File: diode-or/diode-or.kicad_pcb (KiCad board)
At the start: 2 copper layers, 80.4 x 51.4 mm, 24 parts, among them J1 Conn_01x01, J2 Conn_01x01, J3 Conn_01x01, J4 Conn_01x01, J5 Conn_01x01, Q1 Q_NMOS_GDS, SW1 SW_SPDT, U1 LM5050-1

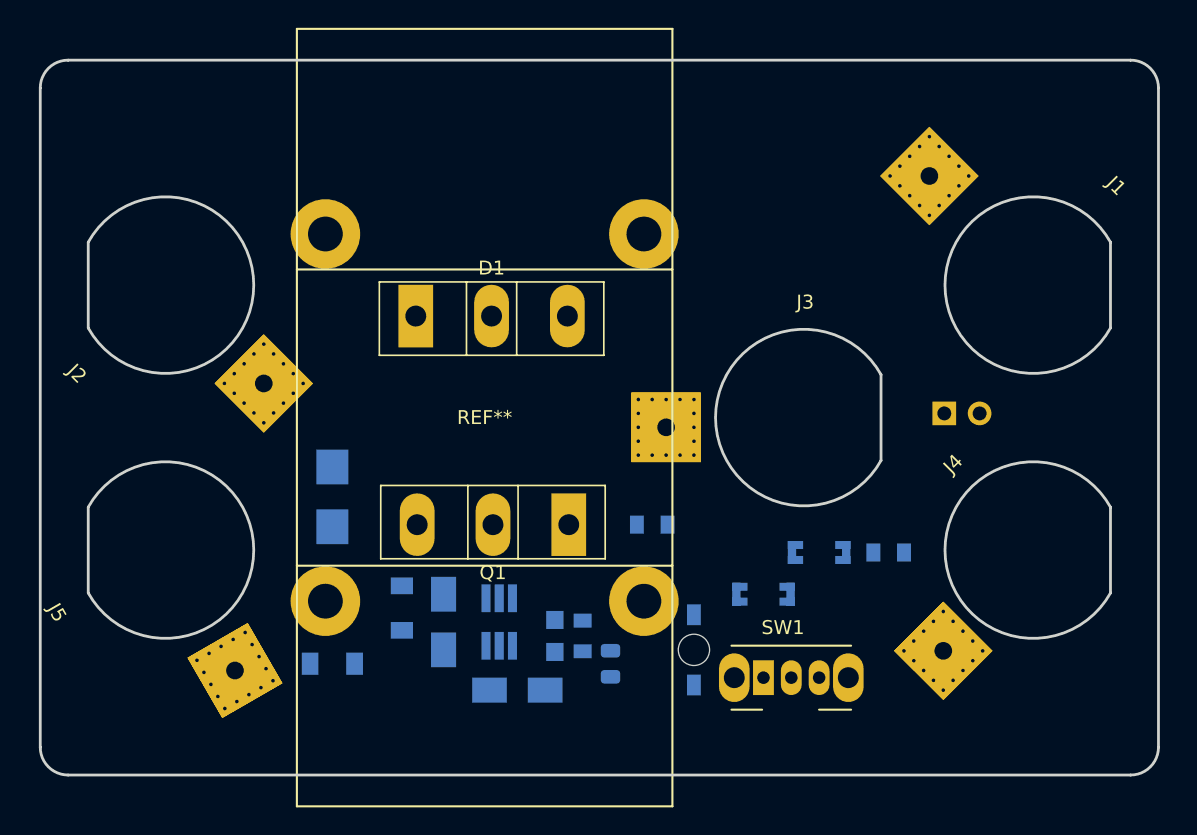
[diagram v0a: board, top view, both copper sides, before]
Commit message: Routed diode-or board. Add generated files.
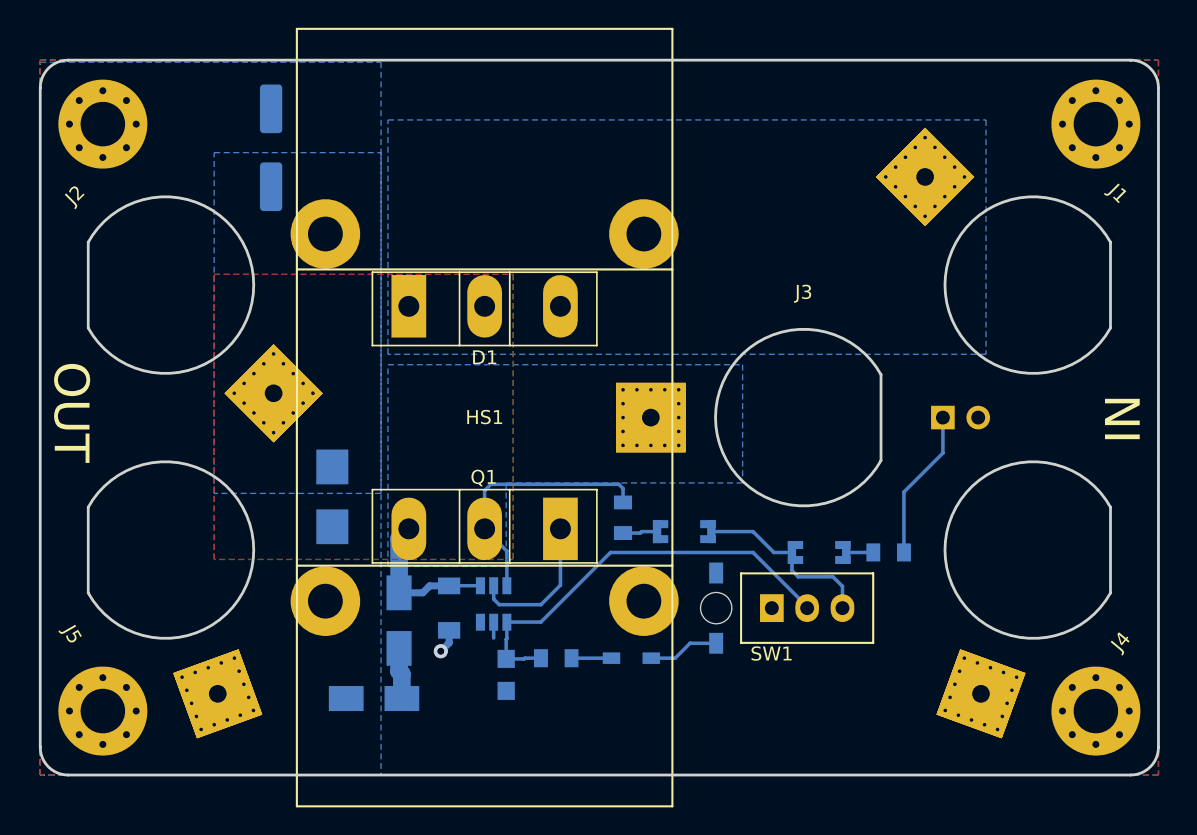
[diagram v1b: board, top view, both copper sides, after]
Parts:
- removed REF**: MA-301-27E, local:MA-301-27E
- added H1: MountingHole_Pad, MountingHole:MountingHole_3.2mm_M3_Pad_Via, F.Cu at (124.5, 73.2)
- added H2: MountingHole_Pad, MountingHole:MountingHole_3.2mm_M3_Pad_Via, F.Cu at (195.9, 73.2)
- added H3: MountingHole_Pad, MountingHole:MountingHole_3.2mm_M3_Pad_Via, F.Cu at (124.5, 115.4)
- added H4: MountingHole_Pad, MountingHole:MountingHole_3.2mm_M3_Pad_Via, F.Cu at (195.9, 115.4)
- added HS1: Heatsink_Pad, local:MA-301-27E, F.Cu at (152.0, 94.3)
- C1: footprint local:C_1206_HandSoldering -> Capacitor_SMD:CP_Elec_6.3x5.9
- C3: value 10uF -> 1uF
- D7: value D_Zener -> MM3Z4V3T1G; footprint Diode_SMD:D_0805_2012Metric -> local:SOD-323_477-02-H_HandSoldering
- J1, J2, J3: value Conn_01x01 -> Binding Post (RED)
- J4, J5: value Conn_01x01 -> Binding Post (BLACK)
- Q1: value Q_NMOS_GDS -> IRFP4710PBF
- SW1: footprint Button_Switch_THT:SW_CuK_OS102011MA1QN1_SPDT_Angled -> local:ASE1D-2M-10-Z
- U1: footprint Package_TO_SOT_SMD:TSOT-23-6_HandSoldering -> Package_TO_SOT_SMD:TSOT-23-6
- moved C1 37.4 mm to (136.6, 74.9), turned to 90 degrees
- moved D6 10.3 mm to (144.0, 114.5), turned to 0 degrees
- moved D3 7.26 mm to (166.3, 102.5)
- moved SW1 5.04 mm to (172.6, 108.0)
- moved C2 4.48 mm to (153.5, 112.8)
- moved C3 3.40 mm to (149.4, 108.0)
- moved D8 3.40 mm to (168.6, 108.0)
- moved D4 3.20 mm to (145.8, 108.9)
- moved R3 2.48 mm to (157.1, 111.6), turned to 0 degrees
- moved R1 2.16 mm to (161.9, 101.5), turned to 270 degrees
- moved D7 1.55 mm to (162.5, 111.6), turned to 0 degrees
- moved U1 1.36 mm to (152.6, 107.7)
- moved J1 0.87 mm to (191.4, 84.8)
- moved D1 0.86 mm to (146.5, 86.3)
- moved J3 0.71 mm to (174.9, 94.3)
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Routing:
- net /VS: track 0.00 -> 30.6 mm
- net /OUT_P: track 0.00 -> 18.8 mm
- net /VS_OR: track 0.00 -> 13.4 mm
- net /IN_FET_P: track 0.00 -> 11.0 mm
- net /BATT: track 0.00 -> 10.9 mm
- net /GATE: track 0.00 -> 10.6 mm
- net Net-(D7-Pad2): track 0.00 -> 5.12 mm
- net GND: track 0.00 -> 4.82 mm
- net Net-(D7-Pad1): track 0.00 -> 2.87 mm
- net Net-(D3-Pad2): track 0.00 -> 2.49 mm
- net Net-(D5-Pad2): track 0.00 -> 1.95 mm
- net /IN_OUT_N: track 0.00 -> 1.75 mm, vias 0 -> 1
- added copper zone on B.Cu, net /IN_D_P
- added copper zone on B.Cu, net /IN_FET_P
- added copper zone on B.Cu, net /IN_OUT_N
- added copper zone on F.Cu, net /IN_OUT_N
- added copper zone on B.Cu, net /OUT_P
- added copper zone on F.Cu, net /OUT_P
- added copper zone on B.Cu, net GND
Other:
- net class Power added: clearance 0.635, trace_width 0.254, via_dia 0.762, via_drill 0.381
- board text added: "IN"
- board text added: "OUT"

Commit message: Changes to courtyard and pad connection settings.
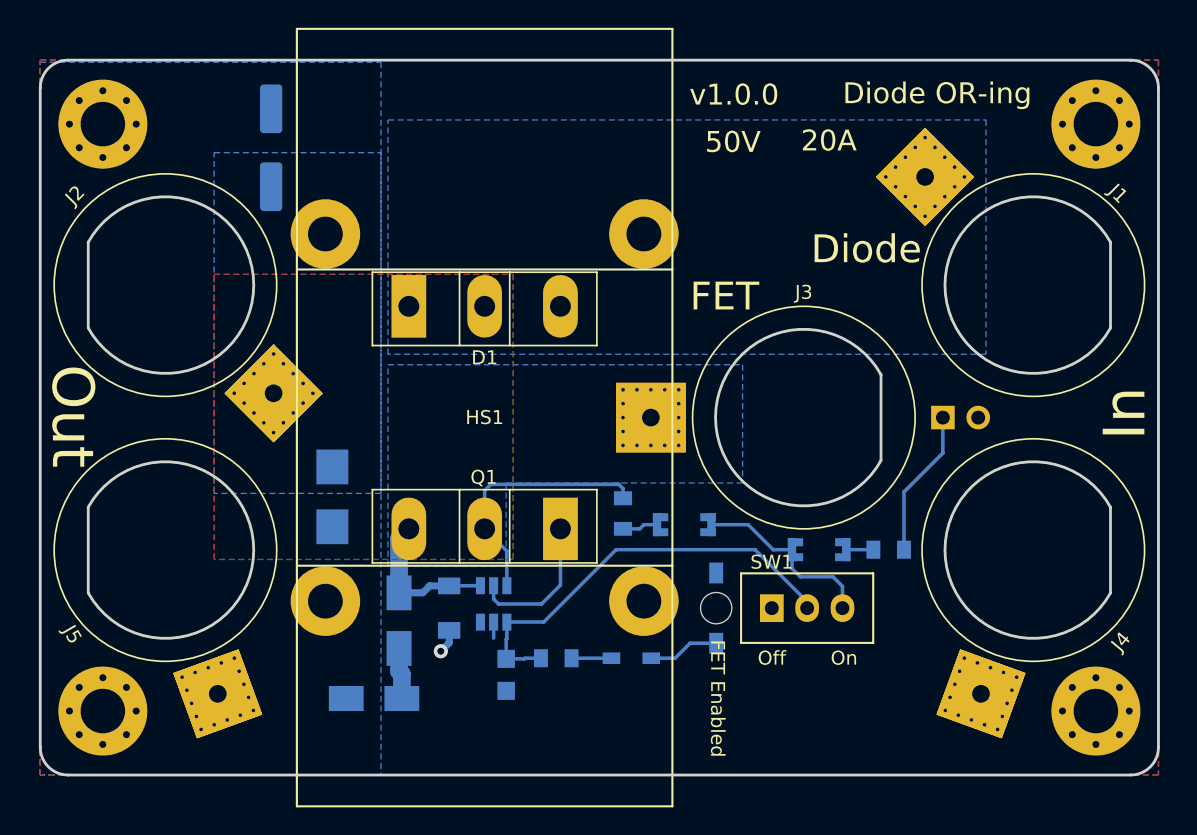
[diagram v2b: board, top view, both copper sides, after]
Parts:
- moved D3 0.50 mm to (166.3, 102.0)
- moved R1 0.30 mm to (161.9, 101.2)
- moved D5 0.20 mm to (176.0, 103.8)
- moved R2 0.20 mm to (181.0, 103.8)
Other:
- board text added: "20A"
- board text added: "50V"
- board text added: "Diode"
- board text added: "Diode OR-ing"
- board text added: "FET"
- board text added: "FET Enabled"
- board text added: "In"
- board text added: "Off"
- board text added: "On"
- board text added: "Out"
- board text added: "v1.0.0"
- board text removed: "IN"
- board text removed: "OUT"
